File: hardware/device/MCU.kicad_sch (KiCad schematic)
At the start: 20 parts, among them J4 EXPANSION, SW24 NRST, U18 STM32H743ZIT6

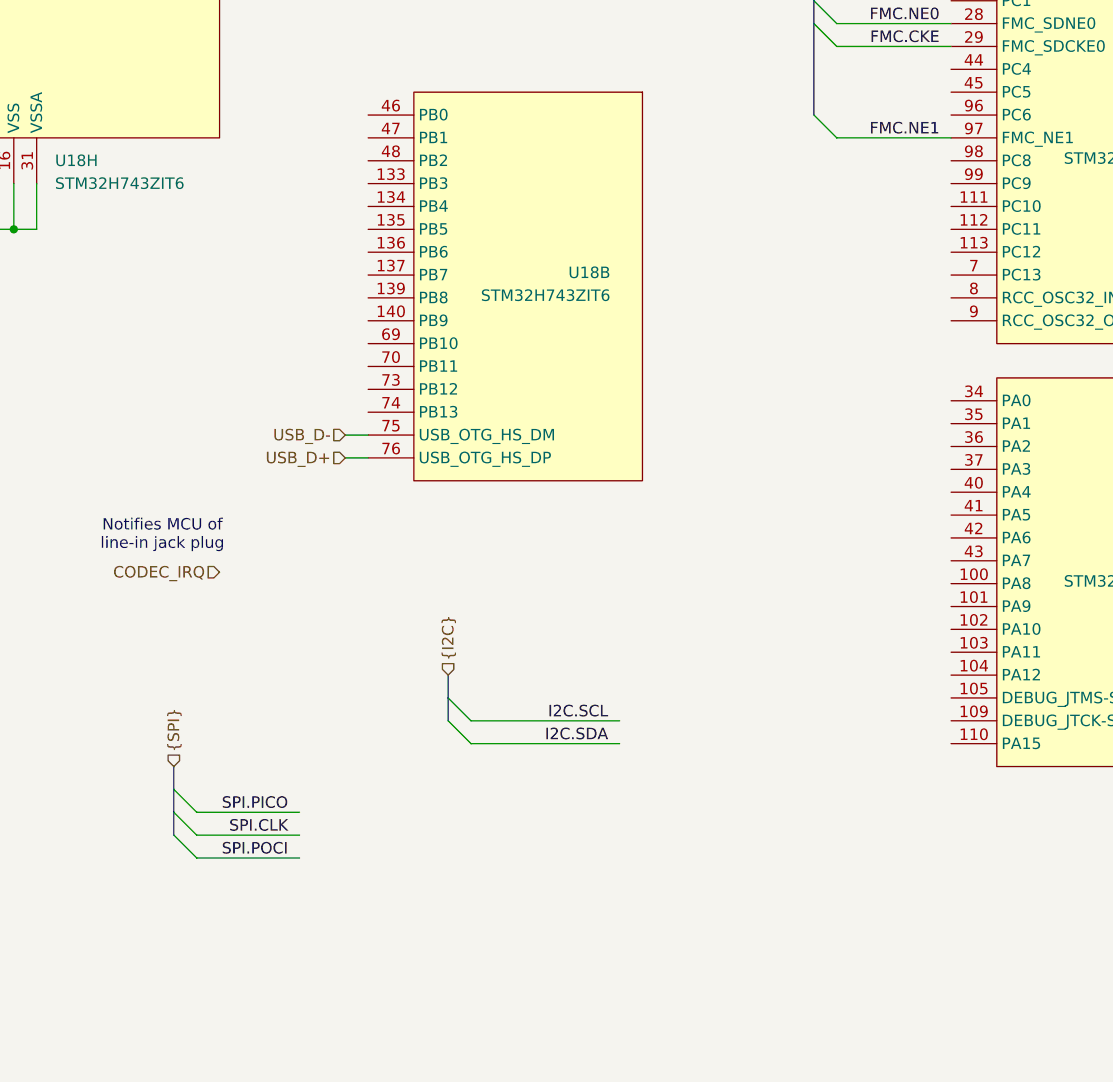
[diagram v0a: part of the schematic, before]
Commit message: feat: add BMPU debug connector
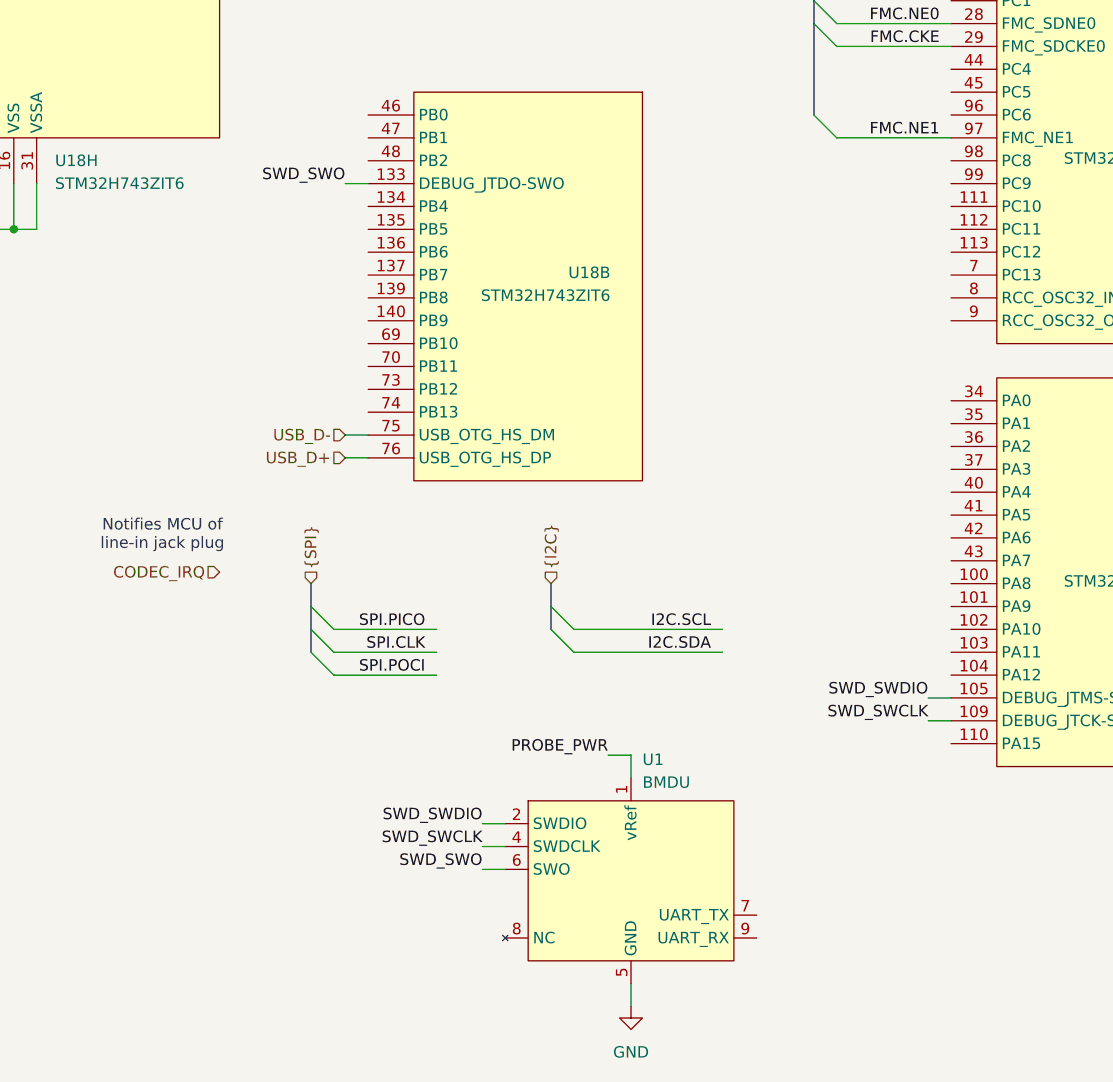
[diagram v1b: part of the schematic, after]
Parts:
- added U1: BMDU, Connector_PinHeader_1.27mm:PinHeader_2x05_P1.27mm_Vertical, symbol pocket_synth:BMDU
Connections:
- net GND: now also U1.3 (GND), U1.5 (GND)
- net SWD_SWDIO: now reaches U18.105 (PA13)
- net SWD_SWDIO: now also U1.2 (SWDIO)
- net SWD_SWCLK: now reaches U18.109 (PA14)
- net SWD_SWCLK: now also U1.4 (SWDCLK)
- net SWD_SWO: now reaches U18.133 (PB3)
- net SWD_SWO: now also U1.6 (SWO)
- new net PROBE_PWR: U1.1 (vRef)

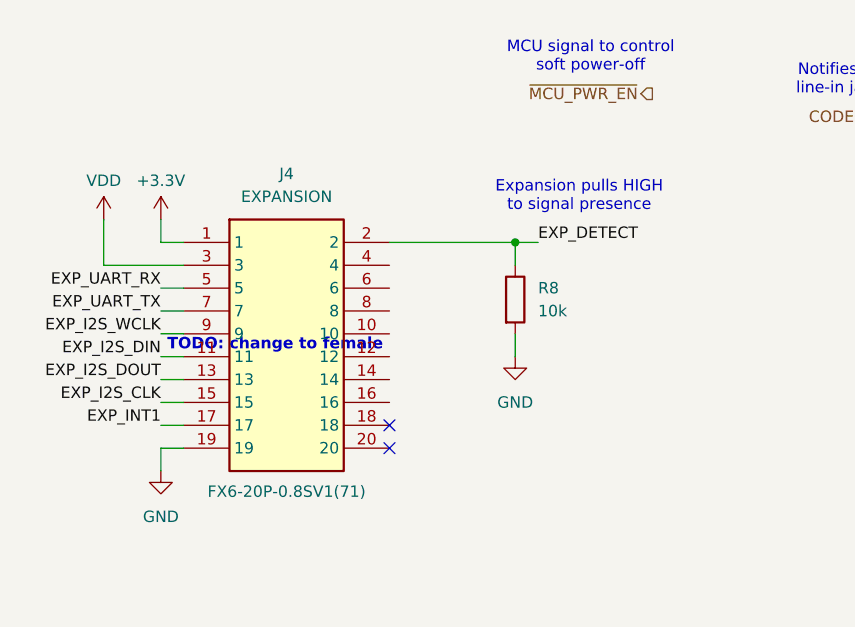
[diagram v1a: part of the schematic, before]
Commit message: feat: add micro SD slot model
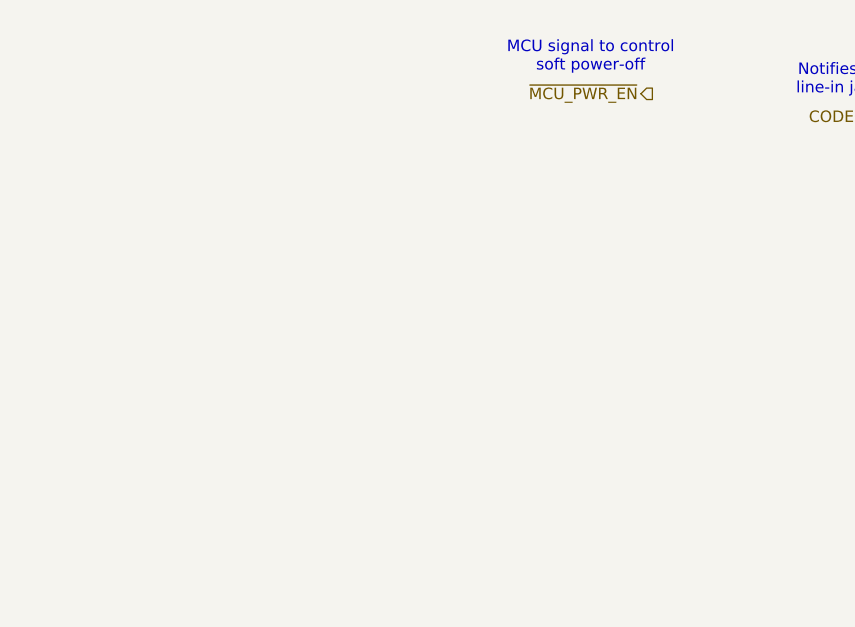
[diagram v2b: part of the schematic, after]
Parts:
- removed J4: EXPANSION, pocket_synth:FX6-20P-0.8SV1(71), symbol pocket_synth:FX6-20P-0.8SV1(71)
- removed R8: 10k, symbol Device:R
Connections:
- no-connect marks 2 -> 0
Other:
- note removed: "Expansion pulls HIGH to signal presence"
- note removed: "TODO: change to female"

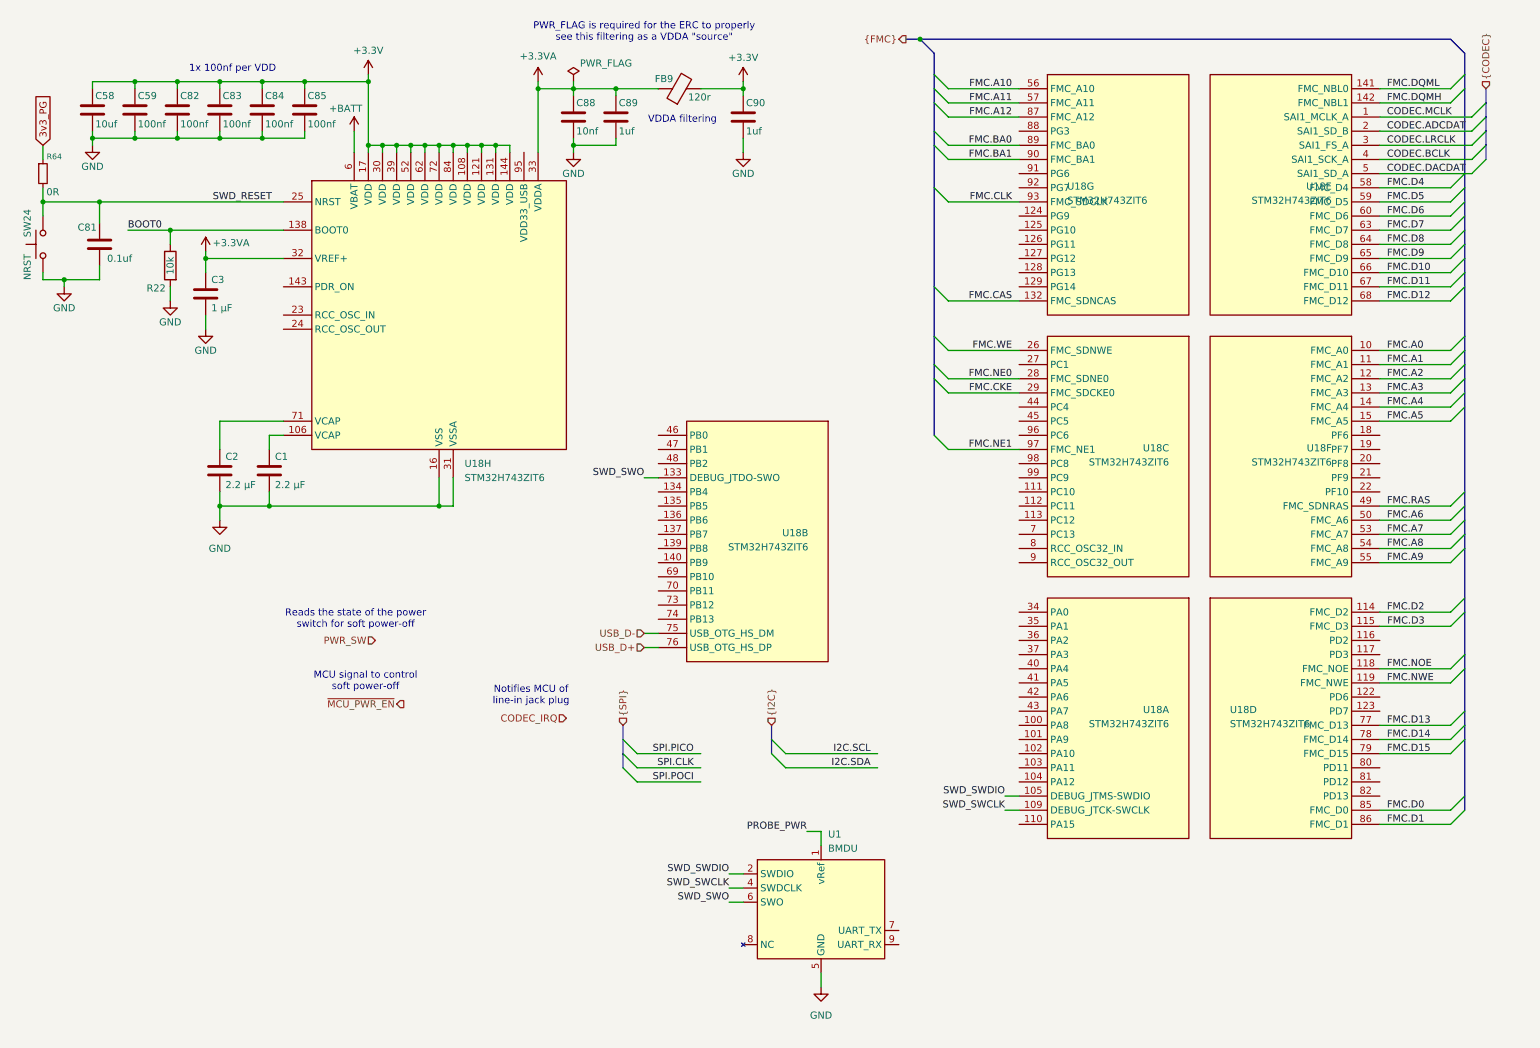
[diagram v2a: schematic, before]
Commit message: feat: fit SD card and SPI bus to layout
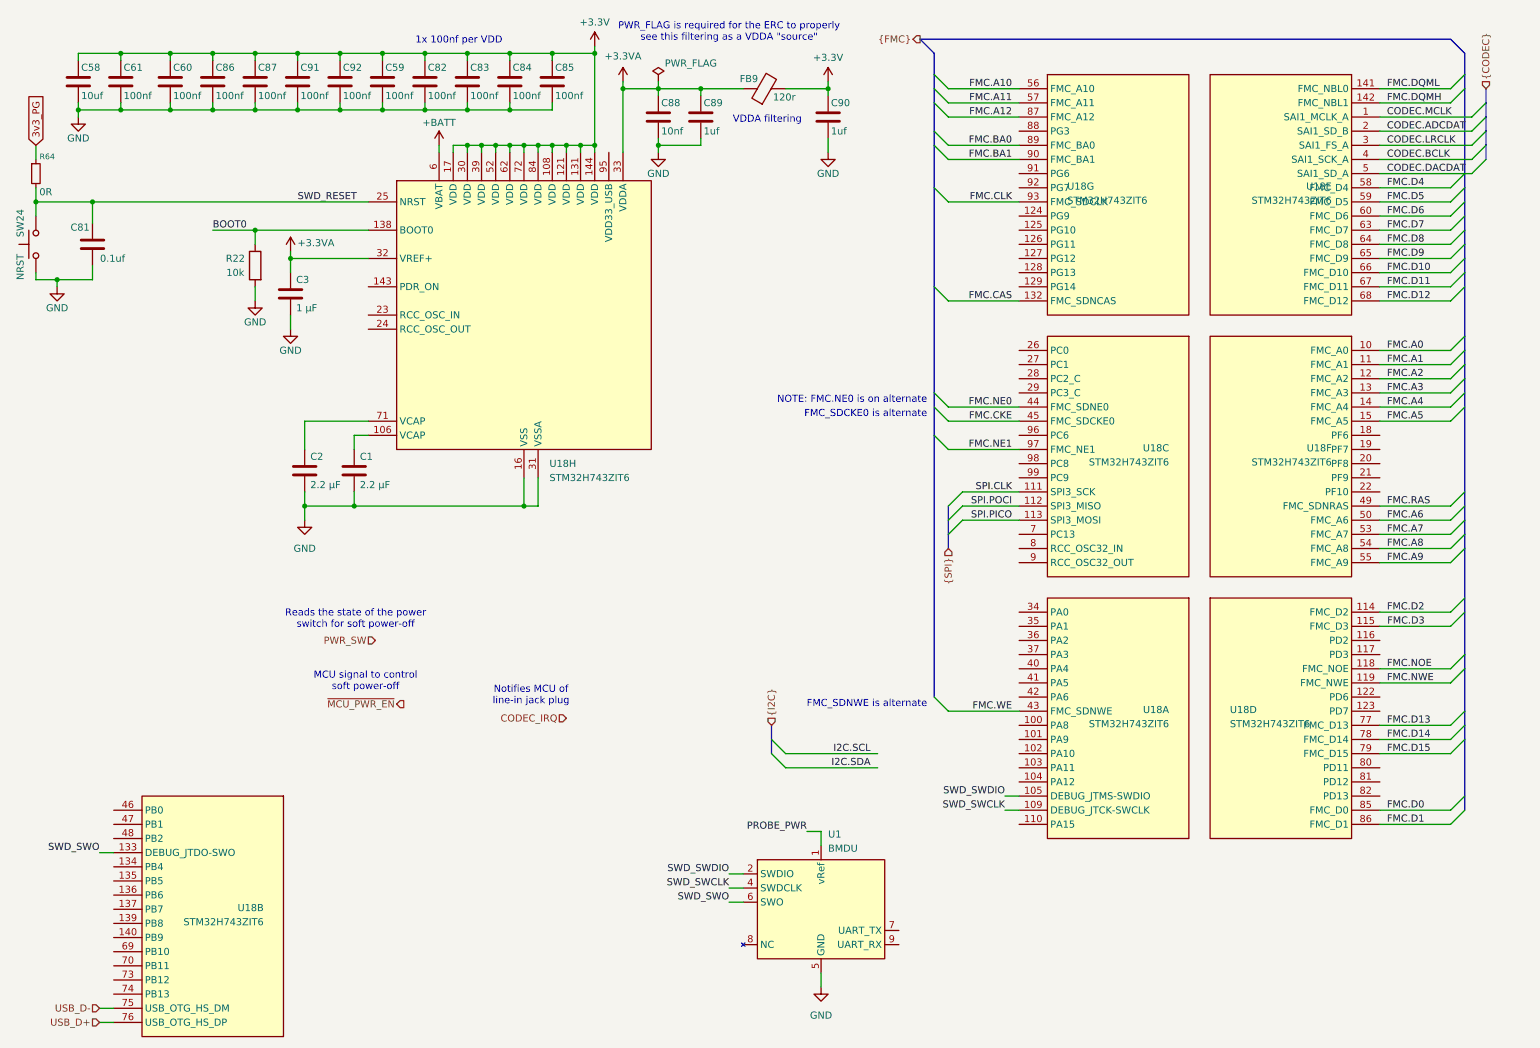
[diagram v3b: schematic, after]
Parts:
- added C60, C61, C86, C91, C92: 100nf, Capacitor_SMD:C_0402_1005Metric, symbol Device:C
- added C87: 100nf, Capacitor_SMD:C_0201_0603Metric, symbol Device:C
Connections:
- net +3.3V: now also C60.1, C61.1, C86.1, C87.1, C91.1, C92.1
- net FMC.CKE: now also U18.45 (PC5); no longer U18.29 (PC3_C)
- net FMC.NE0: now also U18.44 (PC4); no longer U18.28 (PC2_C)
- net FMC.WE: now also U18.43 (PA7); no longer U18.26 (PC0)
- net GND: now also C60.2, C61.2, C86.2, C87.2, C91.2, C92.2
- net SPI.CLK: now also U18.111 (PC10)
- net SPI.PICO: now also U18.113 (PC12)
- net SPI.POCI: now also U18.112 (PC11)
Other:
- note added: "FMC_SDCKE0 is alternate"
- note added: "FMC_SDNWE is alternate"
- note added: "NOTE: FMC.NE0 is on alternate"
- moved on the sheet: C1, C2, C3, C58, C59, C81, C82, C83, C84, C85, C88, C89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

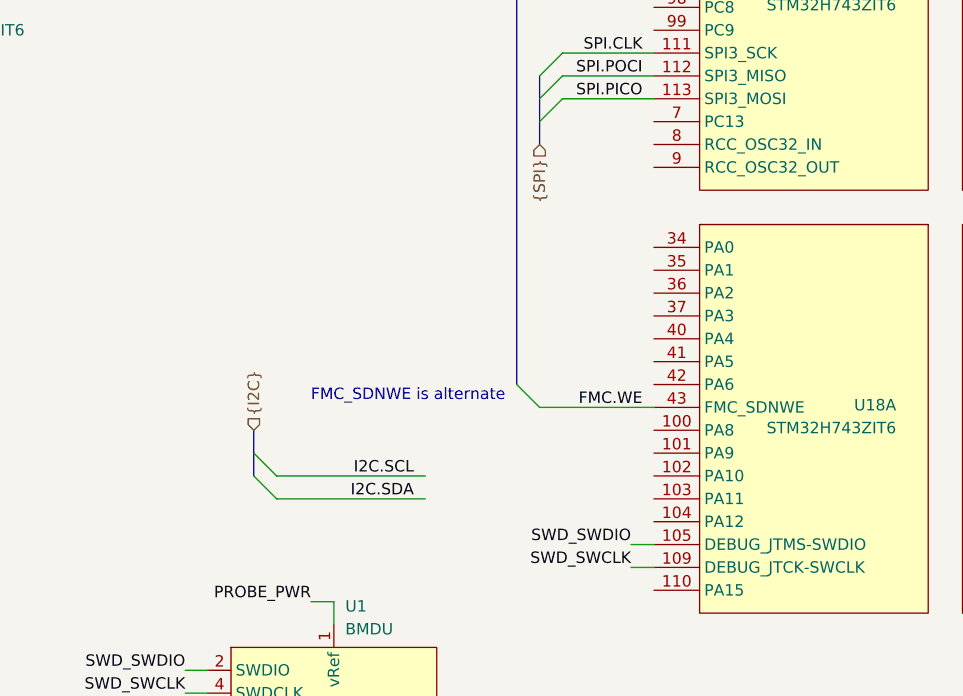
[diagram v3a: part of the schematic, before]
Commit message: chore: audio routing and UART port mapping
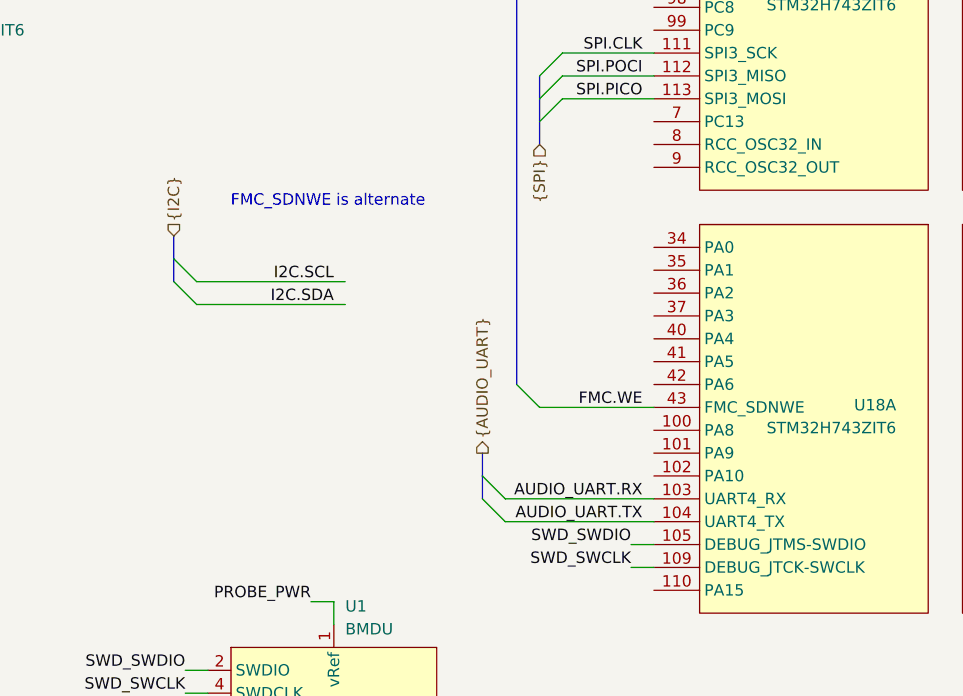
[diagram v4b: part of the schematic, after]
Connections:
- net AUDIO_UART.RX: now reaches U18.103 (PA11)
- net AUDIO_UART.TX: now reaches U18.104 (PA12)
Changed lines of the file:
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@@
 	(generator_version "9.0")
 	(paper "A4")
+	(bus_alias "AUDIO_UART"
+		(members "AUDIO_UART.RX" "AUDIO_UART.TX")
+	)
 	(bus_alias "CODEC"
 		(members "CODEC.MCLK" "CODEC.ADCDAT" "CODEC.LRCLK" "CODEC.BCLK" "CODEC.DACDAT")
@@
 	)
 	(bus_alias "SPI"
-		(members "SPI.CLK" "SPI.POCI" "SPI.PICO")
+		(members "FMC.DQML" "FMC.DQMH" "FMC.CLK" "FMC.CAS" "FMC.RAS" "FMC.D[0..15]"
+			"FMC.A[0..12]" "FMC.NOE" "FMC.NWE" "FMC.BA0" "FMC.BA1" "FMC.CLK" "FMC.CAS"
+			"FMC.WE" "FMC.NE0" "FMC.CKE" "FMC.NE1"
+		)
 	)
 	(text "MCU signal to control\nsoft power-off"
@@
 	(text "FMC_SDNWE is alternate\n"
 		(exclude_from_sim no)
-		(at 179.07 138.43 0)
+		(at 170.18 116.84 0)
 		(effects
 			(font
@@
 	)
 	(bus_entry
-		(at 153.67 149.86)
+		(at 144.78 128.27)
 		(size -2.54 -2.54)
 		(stroke
@@
 	)
 	(bus_entry
+		(at 176.53 147.32)
+		(size 2.54 2.54)
+		(stroke
+			(width 0)
+			(type default)
+		)
+	)
+	(bus_entry
 		(at 273.05 53.34)
 		(size 2.54 -2.54)
@@
 	)
 	(bus_entry
-		(at 153.67 147.32)
+		(at 144.78 125.73)
 		(size -2.54 -2.54)
 		(stroke
@@
 	)
 	(bus_entry
+		(at 179.07 152.4)
+		(size -2.54 -2.54)
+		(stroke
+			(width 0)
+			(type default)
+		)
+	)
+	(bus_entry
 		(at 276.86 40.64)
 		(size 2.54 -2.54)
@@
 	(bus
 		(pts
-			(xy 151.13 144.78) (xy 151.13 147.32)
+			(xy 142.24 123.19) (xy 142.24 125.73)
 		)
 		(stroke
@@
 		)
 	)
+	(bus
+		(pts
+			(xy 176.53 147.32) (xy 176.53 149.86)
+		)
+		(stroke
+			(width 0)
+			(type default)
+		)
+	)
+	(bus
+		(pts
+			(xy 176.53 144.78) (xy 176.53 147.32)
+		)
+		(stroke
+			(width 0)
+			(type default)
+		)
+	)
 	(wire
 		(pts
@@
 	(bus
 		(pts
-			(xy 151.13 142.24) (xy 151.13 144.78)
+			(xy 142.24 120.65) (xy 142.24 123.19)
 		)
 		(stroke
@@
 	(wire
 		(pts
-			(xy 153.67 149.86) (xy 170.18 149.86)
+			(xy 144.78 128.27) (xy 161.29 128.27)
 		)
 		(stroke
@@
 	(wire
 		(pts
-			(xy 153.67 147.32) (xy 170.18 147.32)
+			(xy 144.78 125.73) (xy 161.29 125.73)
 		)
 		(stroke
@@
 		)
 	)
+	(wire
+		(pts
+			(xy 179.07 152.4) (xy 195.58 152.4)
+		)
+		(stroke
+			(width 0)
+			(type default)
+		)
+	)
 	(bus
 		(pts
@@
 	(wire
 		(pts
+			(xy 179.07 149.86) (xy 195.58 149.86)
+		)
+		(stroke
+			(width 0)
+			(type default)
+		)
+	)
+	(wire
+		(pts
 			(xy 78.74 58.42) (xy 64.77 58.42)
 		)
@@
 		)
 	)
+	(label "AUDIO_UART.RX"
+		(at 194.31 149.86 180)
+		(effects
+			(font
+				(size 1.27 1.27)
+			)
+			(justify right bottom)
+		)
+	)
 	(label "FMC.NE1"
 		(at 194.31 92.71 180)
@@
 	)
 	(label "I2C.SDA"
-		(at 168.91 149.86 180)
+		(at 160.02 128.27 180)
 		(effects
 			(font
@@
 	)
 	(label "I2C.SCL"
-		(at 168.91 147.32 180)
+		(at 160.02 125.73 180)
 		(effects
 			(font
@@
 		)
 	)
+	(label "AUDIO_UART.TX"
+		(at 194.31 152.4 180)
+		(effects
+			(font
+				(size 1.27 1.27)
+			)
+			(justify right bottom)
+		)
+	)
 	(label "FMC.DQML"
 		(at 261.62 27.94 0)
@@
 		)
 	)
+	(hierarchical_label "{AUDIO_UART}"
+		(shape output)
+		(at 176.53 144.78 90)
+		(effects
+			(font
+				(size 1.27 1.27)
+			)
+			(justify left)
+		)
+	)
 	(hierarchical_label "USB_D-"
 		(shape input)
@@
 	(hierarchical_label "{I2C}"
 		(shape input)
-		(at 151.13 142.24 90)
+		(at 142.24 120.65 90)
 		(effects
 			(font
@@
 		)
 		(pin "103"
-			(alternate "PA11")
+			(alternate "UART4_RX")
 		)
 		(pin "104"
-			(alternate "PA12")
+			(alternate "UART4_TX")
 		)
 		(pin "105"
